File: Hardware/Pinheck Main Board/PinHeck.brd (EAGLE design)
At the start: 359.2 x 152.3 mm, 418 parts, among them IC2 PIC32MX795F512L-80I/PT, IC3 CD74HCT244E, IC4 CD74HCT244E, IC5 ULN2803A, J1 N/A, U1 P8X32A-Q44, U10 74HCT2G04GV,125, U11 74HC165D-Q100,118, U12 74HC165D-Q100,118, U13 CAT24M01LI-G, U14 MC74HC08ADR2G, U15 MC74HC08ADR2G, U16 MC74HC08ADR2G, U17 MC74HC08ADR2G, U18 MC74HC08ADR2G, U19 MC74HC08ADR2G, U2 DS1340Z-33+, U20 TIP107, U21 TIP107, U22 TIP107, U23 TIP107, U24 TIP107, U25 TIP107, U26 TIP107, U27 TIP107, U28 TIP102, U29 TIP102, U3 CD74HC595M96, U30 TIP102, U31 TIP102, U32 TIP102, U33 TIP102, U34 TIP102, U35 TIP102, U36 WS2801, U38 WS2801, U39 NCP1117DT33G, U4 CAT24M01LI-G, U5 CD74HC595M96, U52 CD74HC123M96, U6 TPS259251, U7 TPS259261, X1 FQ7050B-8.000, X2 9C-6.500MAAJ-T, X3 ABS25-32.768KHz-1-T

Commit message: Test points almost done!
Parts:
- removed TP5, TP6, TP7, TP8: (no value), PP_Connectors:100MIL_TP
- added 12V, 5V, BACK_OUT, COIN_OUT, DMD_1, DMD_11, DMD_13, DMD_3, DMD_5, DMD_7, DMD_9, DOOR_OUT, ENTER_OUT, EXT_RGB_CLK, EXT_RGB_DATA, GI15_, GI_R_0, GI_R_1, GI_R_10, GI_R_11, GI_R_12, GI_R_13, GI_R_14, GI_R_2, GI_R_3, GI_R_4, GI_R_5, GI_R_6, GI_R_7, GI_R_8, GI_R_9, GND, LIGHT_C_0, LIGHT_C_1, LIGHT_C_2, LIGHT_C_3, LIGHT_C_4, LIGHT_C_5, LIGHT_C_6, LIGHT_C_7, LIGHT_R_0, LIGHT_R_1, LIGHT_R_2, LIGHT_R_3, LIGHT_R_4, LIGHT_R_5, LIGHT_R_6, LIGHT_R_7, L_FLIP_OUT, OPTO_1_, OPTO_2_, OPTO_3_, OPTO_4_, OPTO_5_, OPTO_6_, OPTO_7_, PROP_AUX0, PROP_AUX1, RGB_BOUT_L, RGB_BOUT_R, RGB_GOUT_L, RGB_GOUT_R, RGB_ROUT_L, RGB_ROUT_R, R_FLIP_OUT, SD_CS, SD_DI, SD_DO, SD_SCLK, SERVO_0_, SERVO_1_, SERVO_2_, SERVO_3_, SERVO_4_, ST_BU_OUT, ST_LI_, S_L, S_R, TILT_OUT, USER_0_OUT: (no value), PP_Connectors:100MIL_TP
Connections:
- removed net N$16: TP5.P$1, TP6.P$1, TP7.P$1, TP8.P$1
- net 12V_IN: now also 12V.P$1
- net 5V_IN: now also 5V.P$1
- net BACK_OUT: now also BACK_OUT.P$1
- net COIN_OUT: now also COIN_OUT.P$1
- net DMD_1: now also DMD_1.P$1
- net DMD_11: now also DMD_11.P$1
- net DMD_13: now also DMD_13.P$1
- net DMD_3: now also DMD_3.P$1
- net DMD_5: now also DMD_5.P$1
- net DMD_7: now also DMD_7.P$1
- net DMD_9: now also DMD_9.P$1
- net DOOR_OUT: now also DOOR_OUT.P$1
- net ENTER_OUT: now also ENTER_OUT.P$1
- net EXT_RGB_CLK: now also EXT_RGB_CLK.P$1
- net EXT_RGB_DATA: now also EXT_RGB_DATA.P$1
- net GI15: now also GI15_.P$1
- net GI_R_0: now also GI_R_0.P$1
- net GI_R_1: now also GI_R_1.P$1
- net GI_R_10: now also GI_R_10.P$1
- net GI_R_11: now also GI_R_11.P$1
- net GI_R_12: now also GI_R_12.P$1
- net GI_R_13: now also GI_R_13.P$1
- net GI_R_14: now also GI_R_14.P$1
- net GI_R_2: now also GI_R_2.P$1
- net GI_R_3: now also GI_R_3.P$1
- net GI_R_4: now also GI_R_4.P$1
- net GI_R_5: now also GI_R_5.P$1
- net GI_R_6: now also GI_R_6.P$1
- net GI_R_7: now also GI_R_7.P$1
- net GI_R_8: now also GI_R_8.P$1
- net GI_R_9: now also GI_R_9.P$1
- net GND: now also GND.P$1
- net LIGHT_C_0: now also LIGHT_C_0.P$1
- net LIGHT_C_1: now also LIGHT_C_1.P$1
- net LIGHT_C_2: now also LIGHT_C_2.P$1
- net LIGHT_C_3: now also LIGHT_C_3.P$1
- net LIGHT_C_4: now also LIGHT_C_4.P$1
- net LIGHT_C_5: now also LIGHT_C_5.P$1
- net LIGHT_C_6: now also LIGHT_C_6.P$1
- net LIGHT_C_7: now also LIGHT_C_7.P$1
- net LIGHT_R_0: now also LIGHT_R_0.P$1
- net LIGHT_R_1: now also LIGHT_R_1.P$1
- net LIGHT_R_2: now also LIGHT_R_2.P$1
- net LIGHT_R_3: now also LIGHT_R_3.P$1
- net LIGHT_R_4: now also LIGHT_R_4.P$1
- net LIGHT_R_5: now also LIGHT_R_5.P$1
- net LIGHT_R_6: now also LIGHT_R_6.P$1
- net LIGHT_R_7: now also LIGHT_R_7.P$1
- net L_FLIP_OUT: now also L_FLIP_OUT.P$1
- net OPTO_1: now also OPTO_1_.P$1
- net OPTO_2: now also OPTO_2_.P$1
- net OPTO_3: now also OPTO_3_.P$1
- net OPTO_4: now also OPTO_4_.P$1
- net OPTO_5: now also OPTO_5_.P$1
- net OPTO_6: now also OPTO_6_.P$1
- net OPTO_7: now also OPTO_7_.P$1
- net PROP_AUX0: now also PROP_AUX0.P$1
- net PROP_AUX1: now also PROP_AUX1.P$1
- net RGB_BOUT_L: now also RGB_BOUT_L.P$1
- net RGB_BOUT_R: now also RGB_BOUT_R.P$1
- net RGB_GOUT_L: now also RGB_GOUT_L.P$1
- net RGB_GOUT_R: now also RGB_GOUT_R.P$1
- net RGB_ROUT_L: now also RGB_ROUT_L.P$1
- net RGB_ROUT_R: now also RGB_ROUT_R.P$1
- net R_FLIP_OUT: now also R_FLIP_OUT.P$1
- net SD_CS: now also SD_CS.P$1
- net SD_DI: now also SD_DI.P$1
- net SD_DO: now also SD_DO.P$1
- net SD_SCLK: now also SD_SCLK.P$1
- net SERVO_0: now also SERVO_0_.P$1
- net SERVO_1: now also SERVO_1_.P$1
- net SERVO_2: now also SERVO_2_.P$1
- net SERVO_3: now also SERVO_3_.P$1
- net SERVO_4: now also SERVO_4_.P$1
- net ST_BU_OUT: now also ST_BU_OUT.P$1
- net ST_LI: now also ST_LI_.P$1
- net S_L: now also S_L.P$1
- net S_R: now also S_R.P$1
- net TILT_OUT: now also TILT_OUT.P$1
- net USER_0_OUT: now also USER_0_OUT.P$1
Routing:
- net 12V: track 685.7 -> 25.5 mm
- net 5V_IN: track 9.76 -> 38.5 mm
- net 12V_IN: track 0.00 -> 19.2 mm
- net GND: track 424.5 -> 431.8 mm
- net OPTO_1: track 10.9 -> 16.7 mm
- net OPTO_2: track 28.9 -> 34.7 mm
- net DMD_13: track 58.6 -> 64.4 mm
- net ST_BU_OUT: track 6.85 -> 12.6 mm
- net ENTER_OUT: track 6.82 -> 12.5 mm
- net L_FLIP_OUT: track 6.82 -> 12.5 mm
- net TILT_OUT: track 6.80 -> 12.5 mm
- net USER_0_OUT: track 6.80 -> 12.5 mm
- net BACK_OUT: track 6.78 -> 12.4 mm
- net COIN_OUT: track 6.76 -> 12.4 mm
- net DMD_1: track 61.3 -> 66.9 mm
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- added copper zone on layer 15, net 12V
- removed copper zone on layer 16, net 12V

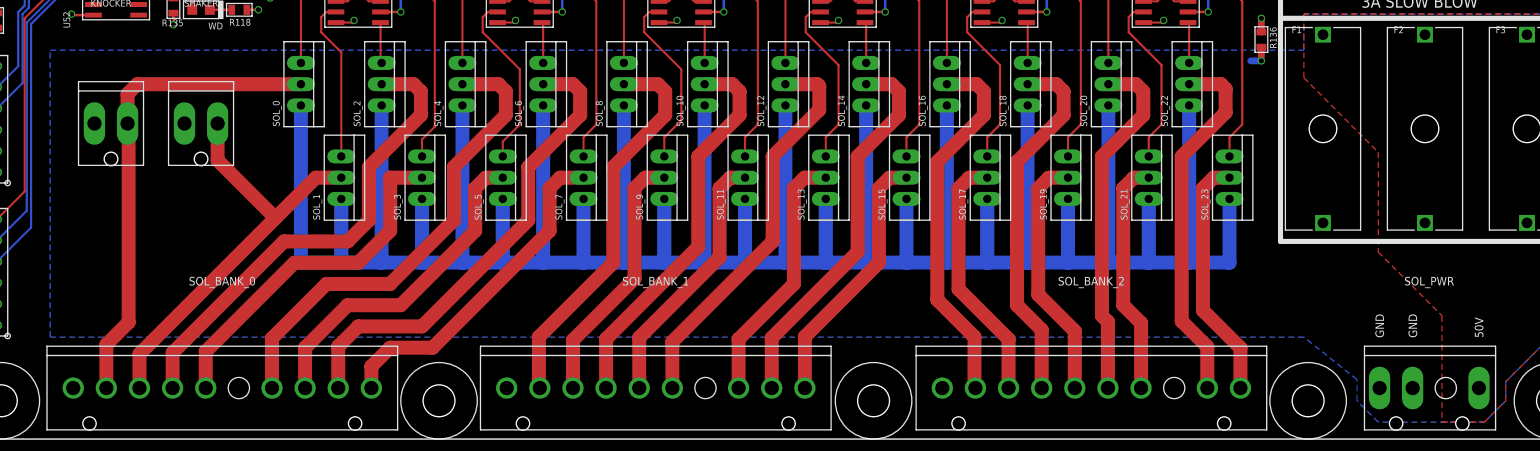
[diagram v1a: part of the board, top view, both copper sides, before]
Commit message: finished test points.
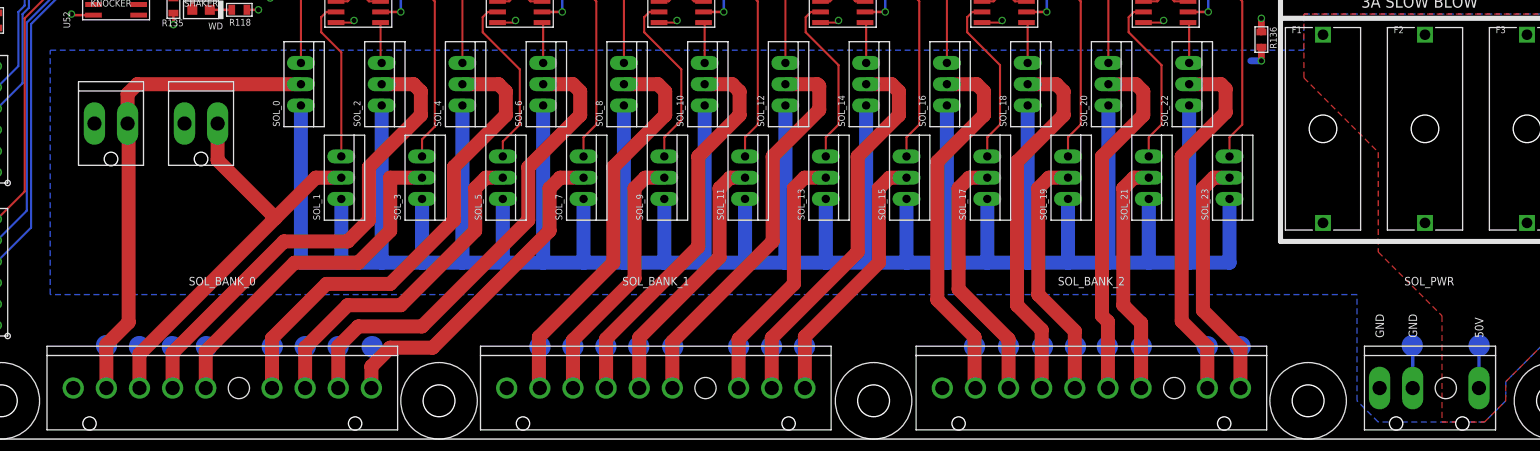
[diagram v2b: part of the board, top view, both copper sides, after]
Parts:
- added 50V, SOL_GND, SOL_PWR_0, SOL_PWR_1, SOL_PWR_10, SOL_PWR_11, SOL_PWR_12, SOL_PWR_13, SOL_PWR_14, SOL_PWR_15, SOL_PWR_16, SOL_PWR_17, SOL_PWR_18, SOL_PWR_19, SOL_PWR_2, SOL_PWR_20, SOL_PWR_21, SOL_PWR_22, SOL_PWR_23, SOL_PWR_3, SOL_PWR_4, SOL_PWR_5, SOL_PWR_6, SOL_PWR_7, SOL_PWR_8, SOL_PWR_9: (no value), PP_Connectors:100MIL_TP
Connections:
- net 50V: now also 50V.P$1
- net SOL_GND: now also SOL_GND.P$1
- net SOL_PWR_0: now also SOL_PWR_0.P$1
- net SOL_PWR_1: now also SOL_PWR_1.P$1
- net SOL_PWR_10: now also SOL_PWR_10.P$1
- net SOL_PWR_11: now also SOL_PWR_11.P$1
- net SOL_PWR_12: now also SOL_PWR_12.P$1
- net SOL_PWR_13: now also SOL_PWR_13.P$1
- net SOL_PWR_14: now also SOL_PWR_14.P$1
- net SOL_PWR_15: now also SOL_PWR_15.P$1
- net SOL_PWR_16: now also SOL_PWR_16.P$1
- net SOL_PWR_17: now also SOL_PWR_17.P$1
- net SOL_PWR_18: now also SOL_PWR_18.P$1
- net SOL_PWR_19: now also SOL_PWR_19.P$1
- net SOL_PWR_2: now also SOL_PWR_2.P$1
- net SOL_PWR_20: now also SOL_PWR_20.P$1
- net SOL_PWR_21: now also SOL_PWR_21.P$1
- net SOL_PWR_22: now also SOL_PWR_22.P$1
- net SOL_PWR_23: now also SOL_PWR_23.P$1
- net SOL_PWR_3: now also SOL_PWR_3.P$1
- net SOL_PWR_4: now also SOL_PWR_4.P$1
- net SOL_PWR_5: now also SOL_PWR_5.P$1
- net SOL_PWR_6: now also SOL_PWR_6.P$1
- net SOL_PWR_7: now also SOL_PWR_7.P$1
- net SOL_PWR_8: now also SOL_PWR_8.P$1
- net SOL_PWR_9: now also SOL_PWR_9.P$1
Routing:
- net SOL_GND: track 430.9 -> 436.0 mm
- net 50V: track 0.00 -> 5.11 mm
- net SOL_PWR_0: track 57.5 -> 62.6 mm
- net SOL_PWR_16: track 44.4 -> 49.5 mm
- net SOL_PWR_18: track 43.6 -> 48.7 mm
- net SOL_PWR_7: track 40.3 -> 45.3 mm
- net SOL_PWR_20: track 42.3 -> 47.4 mm
- net SOL_PWR_3: track 42.6 -> 47.6 mm
- net SOL_PWR_19: track 29.8 -> 34.8 mm
- net SOL_PWR_11: track 31.4 -> 36.4 mm
- net SOL_PWR_12: track 47.5 -> 52.5 mm
- net SOL_PWR_23: track 29.4 -> 34.4 mm
- net SOL_PWR_15: track 31.4 -> 36.4 mm
- net SOL_PWR_21: track 28.3 -> 33.3 mm
- net SOL_PWR_4: track 57.0 -> 62.0 mm
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
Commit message: Layout complete and silkscreen almost done!
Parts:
- added SYM1: HIGH_VOLTAGE_500MIL, PP_Aesthetics:HIGH_VOLTAGE_500MIL
- moved LOGO1 69.3 mm to (164.6, 84.2)
- moved U$2 44.1 mm to (228.3, 118.5)
- moved LIGHT_COL 7.62 mm to (6.35, 105.2)
- moved LIGHT_C_1 7.62 mm to (11.4, 111.1)
- moved LIGHT_C_3 7.62 mm to (11.4, 103.2)
- moved LIGHT_C_5 7.62 mm to (11.4, 95.3)
- moved LIGHT_C_6 7.62 mm to (11.4, 91.3)
- moved LIGHT_C_7 7.62 mm to (11.4, 87.3)
- moved LIGHT_C_0 7.62 mm to (11.4, 115.1)
- moved LIGHT_C_2 7.62 mm to (11.4, 107.1)
- moved LIGHT_C_4 7.62 mm to (11.4, 99.2)
- moved H19 7.37 mm to (4.57, 78.0)
- moved LIGHT_ROW 2.54 mm to (6.35, 46.1)
- moved LIGHT_R_0 2.54 mm to (11.4, 59.9)
- moved LIGHT_R_1 2.54 mm to (11.4, 52.0)
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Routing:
- net LIGHT_C_0: track 27.4 -> 31.1 mm
- net LIGHT_C_7: track 42.8 -> 46.0 mm
- net LIGHT_C_5: track 42.2 -> 45.4 mm
- net LIGHT_C_1: track 41.0 -> 44.1 mm
- net LIGHT_C_6: track 29.6 -> 32.8 mm
- net LIGHT_C_4: track 28.8 -> 31.9 mm
- net LIGHT_C_3: track 41.8 -> 45.0 mm
- net LIGHT_C_2: track 28.2 -> 31.4 mm
- net LIGHT_R_2: track 31.8 -> 29.2 mm
- net LIGHT_R_0: track 29.3 -> 28.2 mm
- net LIGHT_R_7: track 39.8 -> 40.9 mm
- net LIGHT_R_6: track 28.9 -> 27.8 mm
- net LIGHT_R_4: track 29.5 -> 28.5 mm
- net LIGHT_R_3: track 41.2 -> 40.2 mm
- net LIGHT_R_1: track 42.0 -> 41.0 mm
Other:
- board text added: "1"
- board text added: "3.5MM TRS AUDIO"
- board text added: "PIC32 EEPROM"
- board text added: "PROP EEPROM"
- board text added: "PinHeck Addon Board User Logic Optional Universal Slot"
- board text added: "SD CARD AUDIO/VIDEO"
- board text added: "USE CR2032 TYPE BATTERIES ONLY"
- board text removed: "Pin Heck Addon Board / User Logic Optional Universal Slot. PHABULOUS"

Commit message: Silkscreen done.
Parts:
- moved C18 1.78 mm to (67.1, 108.3)
- moved LOGO1 1.02 mm to (164.5, 83.2)
- moved F6 0.92 mm to (125.7, 130.0)
- moved OPTO_2 0.76 mm to (68.3, 145.8)
- moved OPTO_2_ 0.76 mm to (74.3, 140.0)
- moved OPTO_4 0.76 mm to (68.3, 133.1)
- moved OPTO_4_ 0.76 mm to (74.3, 127.8)
- moved OPTO_6 0.76 mm to (68.3, 121.4)
- moved OPTO_6_ 0.76 mm to (74.3, 116.3)
- moved C19 0.38 mm to (113.0, 117.7)
- moved U36 0.25 mm to (173.0, 117.3)
- moved R176 0.13 mm to (222.5, 82.4)
- renumbered J1 to USB_PROG
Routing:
- net SERVO_5V: track 41.2 -> 42.1 mm
- net N$6: track 41.7 -> 42.5 mm
- net OPTO_6: track 33.9 -> 34.6 mm
- net OPTO_4: track 34.4 -> 35.2 mm
- net OPTO_2: track 34.7 -> 35.5 mm
- net N$14: track 44.0 -> 44.8 mm
- net N$11: track 41.7 -> 42.5 mm
- net GND: track 431.8 -> 431.0 mm
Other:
- board text added: "12V SOURCE"
- board text added: "FLASHER FUSE: USE 1A"
- board text added: "GI_0 FUSE: USE 1A"
- board text added: "GI_1 USE 1A"
- board text added: "SERVO FUSE 3A FAST BLOW"

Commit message: REV 7 preliminary done.
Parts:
- added 3.3V: (no value), PP_Connectors:100MIL_TP
- added FID1, FID2, FID3: FIDUCIAL_100MIL, MF_Aesthetics:FIDUCIAL_100MIL
- added FID4, FID5: FIDUCIAL_0.5MM, MF_Aesthetics:FIDUCIAL_0.5MM
- moved C19 0.65 mm to (112.9, 117.1)
- renumbered BOARD_POWER to BOARD_POWER_IN, CABINET to CABINET_I/O, PIC_RST to PIC_RESET, PROP_RST to PROP_RESET, SOL_PWR to SOLENOID_POWER_IN
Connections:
- net 3.3V: now also 3.3V.P$1
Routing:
- net 3.3V: track 244.3 -> 246.7 mm
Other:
- board text added: "GI_1 1A"
- board text added: "REAL TIME CLOCK BATT. CR2032 TYPE ONLY"
- board text removed: "GI_1 USE 1A"
- board text removed: "USE CR2032 TYPE BATTERIES ONLY"

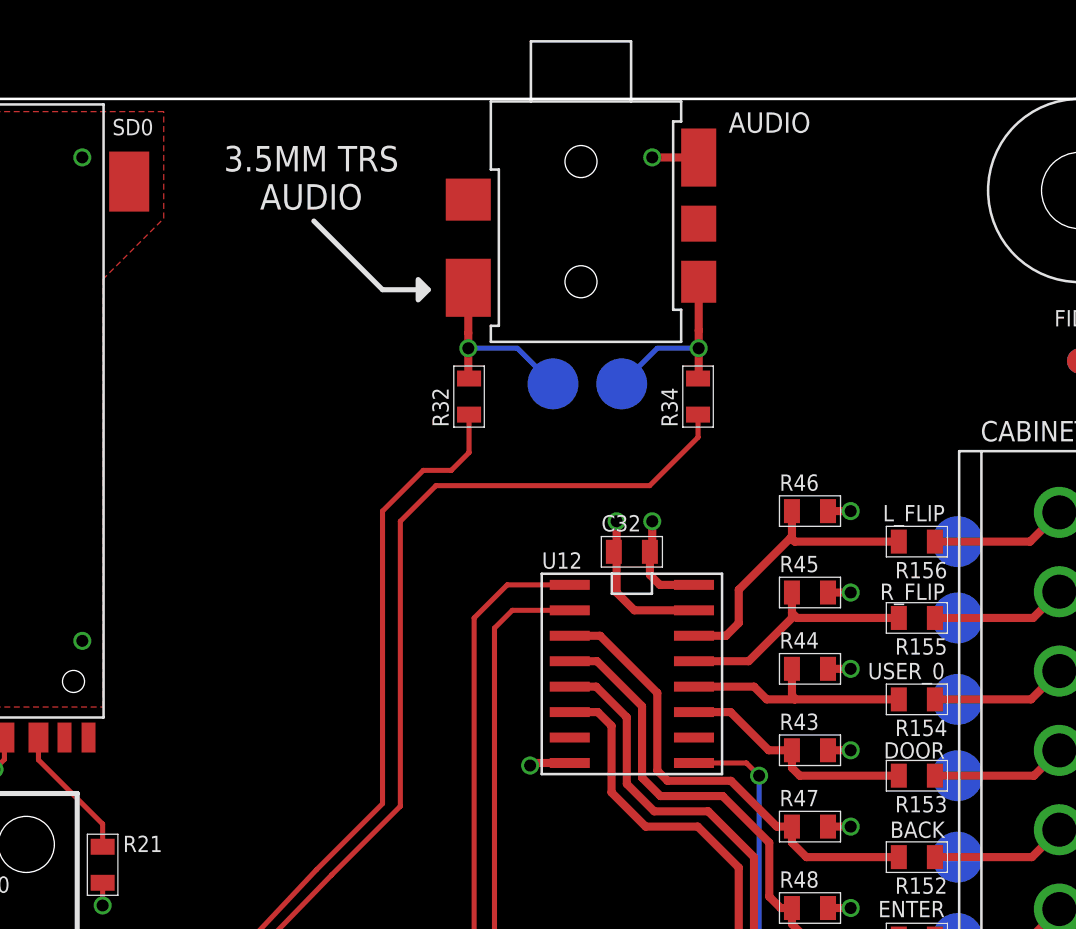
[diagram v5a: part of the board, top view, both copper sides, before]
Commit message: Added AUX power Connector
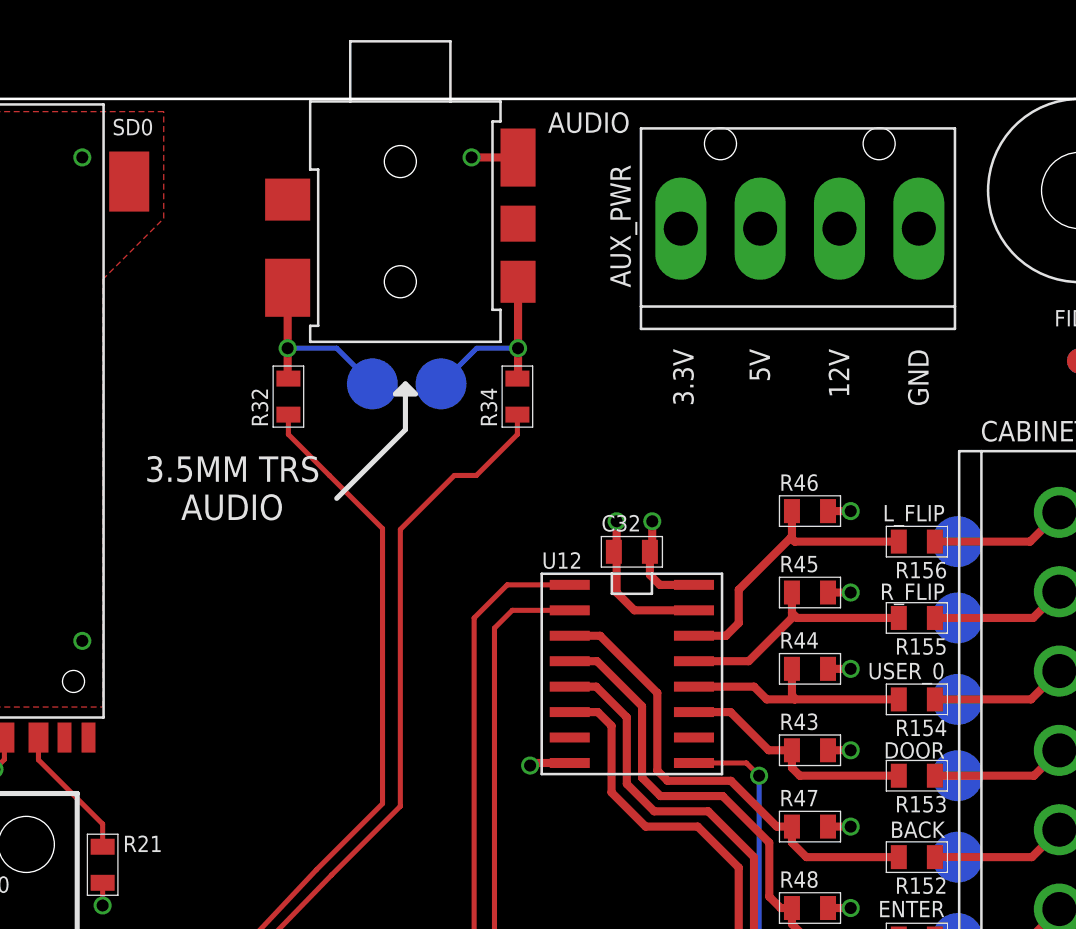
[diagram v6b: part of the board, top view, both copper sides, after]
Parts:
- added AUX_PWR: 26-64-4040, PP_Connectors:26-64-4040
- moved AUDIO 9.02 mm to (320.7, 152.1)
- moved R32 9.02 mm to (315.1, 137.4)
- moved R34 9.02 mm to (326.5, 137.4)
- moved S_L 9.02 mm to (319.3, 138.0)
- moved S_R 9.02 mm to (322.7, 138.0)
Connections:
- net 12V: now also AUX_PWR.2
- net 3.3V: now also AUX_PWR.4
- net 5V: now also AUX_PWR.3
- net GND: now also AUX_PWR.1
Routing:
- net AUD1: track 175.8 -> 166.5 mm
- net AUD0: track 165.0 -> 164.4 mm

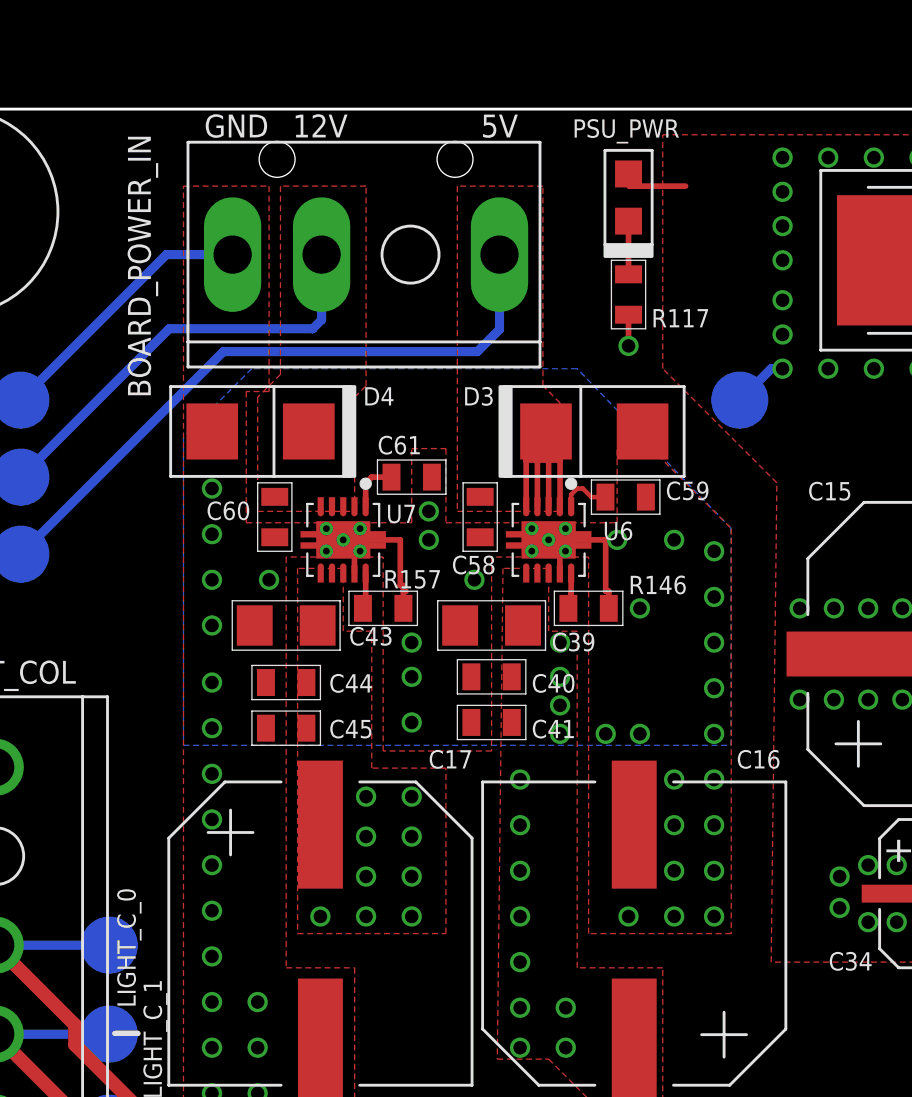
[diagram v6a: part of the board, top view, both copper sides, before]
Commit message: Added 1M pullup to EN pin on the TPS25925x/6x
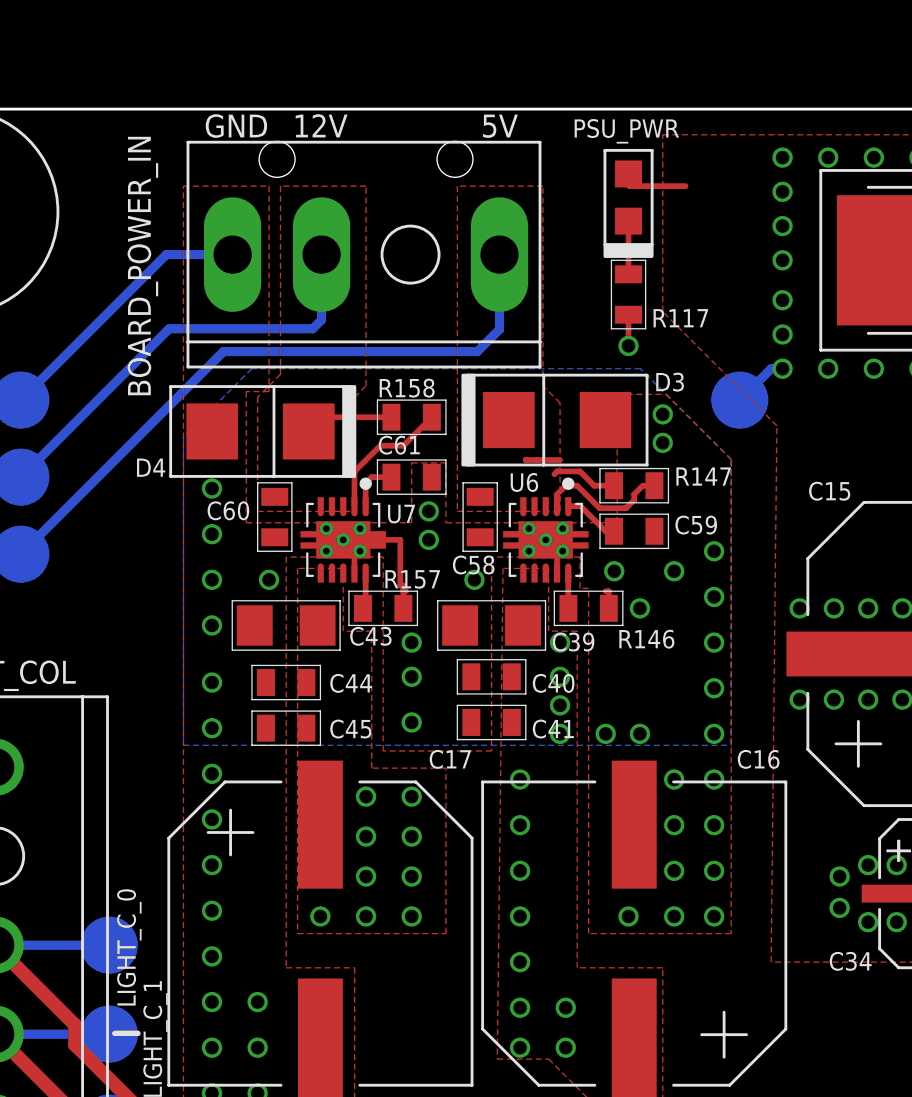
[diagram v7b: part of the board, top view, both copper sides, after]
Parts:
- added R147, R158: 1M, PP_Passives:0805
- moved D3 1.73 mm to (31.4, 138.4)
- moved C59 1.57 mm to (34.8, 133.5)
- moved U6 0.13 mm to (30.9, 133.1)
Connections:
- new net N$16: R147.2, U6.P$2
- new net N$17: R158.2, U7.P$2
- net 12V_IN: now also R158.1; no longer U7.P$2
- net 5V_IN: now also R147.1; no longer U6.P$2
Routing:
- net N$16: track 0.00 -> 6.00 mm
- net N$17: track 0.00 -> 5.99 mm
- net 5V_IN: track 38.5 -> 33.3 mm
- net 12V_IN: track 19.2 -> 23.5 mm
- net GND: track 431.0 -> 426.9 mm, vias 171 -> 173
